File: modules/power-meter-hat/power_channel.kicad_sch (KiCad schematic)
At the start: 8 parts, among them J2 Conn_01x02, U2 INA219AxD

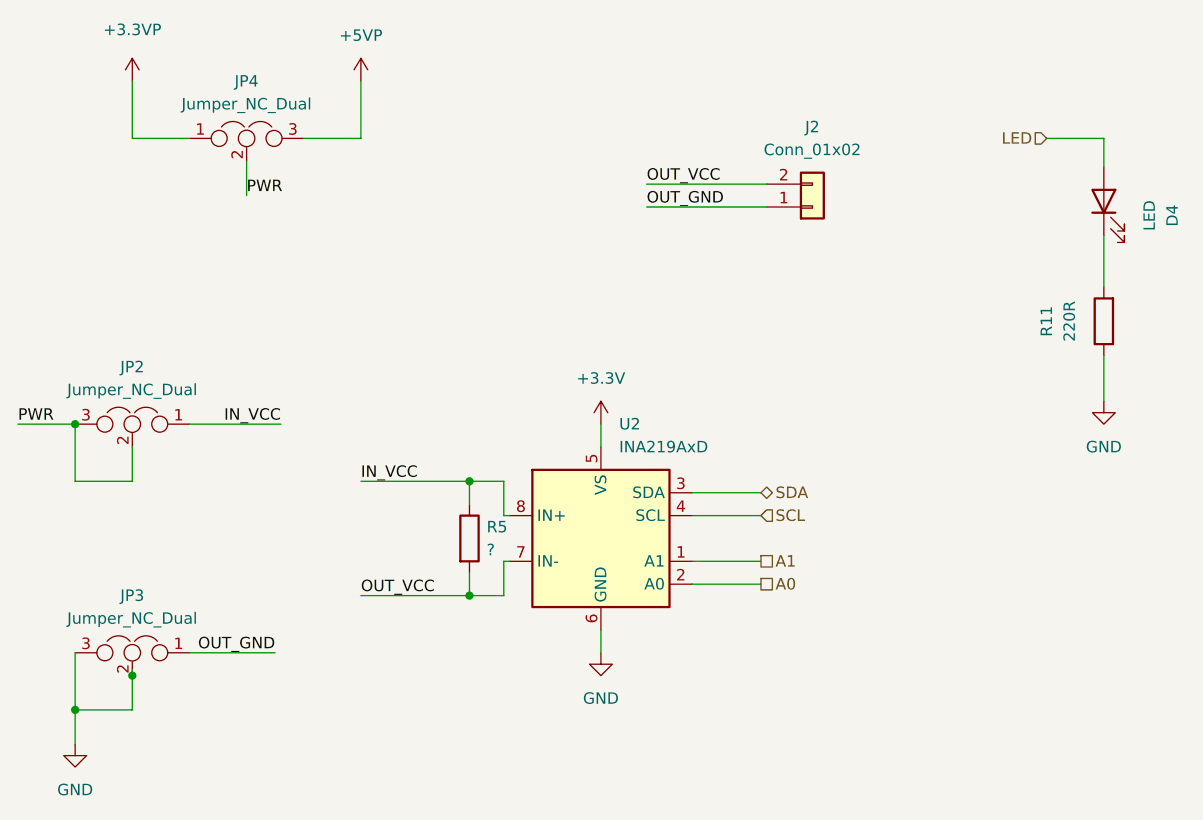
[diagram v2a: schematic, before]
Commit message: Reannotate schematic
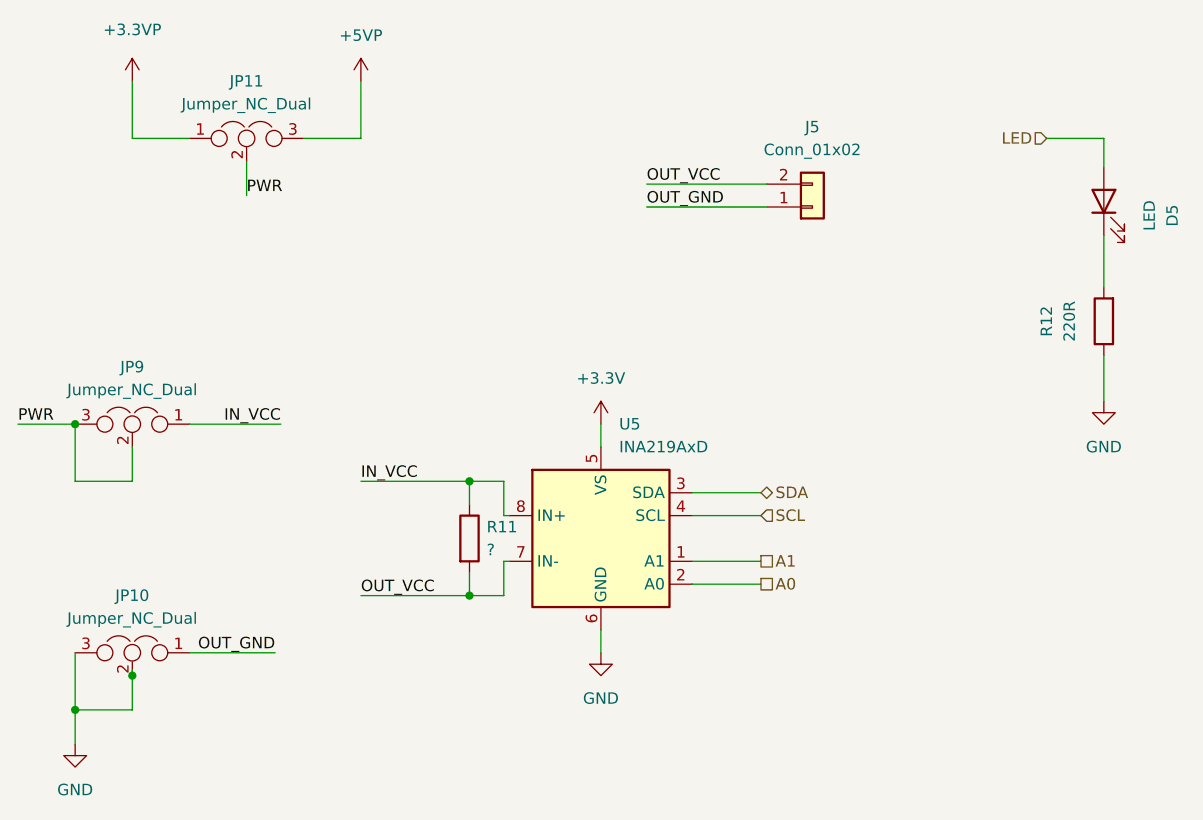
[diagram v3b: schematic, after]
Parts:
- renumbered D4 to D5, J2 to J5, JP3 to JP10, JP4 to JP11, JP2 to JP9, R5 to R11, R11 to R12, U2 to U5
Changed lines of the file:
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@@
   (symbol (lib_id "Device:Jumper_NC_Dual") (at 76.2 63.5 0) (mirror y)
     (in_bom yes) (on_board yes) (fields_autoplaced)
-    (property "Reference" "JP2" (id 0) (at 76.2 57.15 0))
+    (property "Reference" "JP9" (id 0) (at 76.2 57.15 0))
     (property "Value" "Jumper_NC_Dual" (id 1) (at 76.2 59.69 0))
     (property "Footprint" "Connector_PinHeader_2.54mm:PinHeader_1x03_P2.54mm_Vertical" (id 2) (at 76.2 63.5 0)
@@
   (symbol (lib_id "power:+3.3V") (at 128.27 63.5 0)
     (in_bom yes) (on_board yes) (fields_autoplaced)
-    (property "Reference" "#PWR0109" (id 0) (at 128.27 67.31 0)
+    (property "Reference" "#PWR036" (id 0) (at 128.27 67.31 0)
       (effects (font (size 1.27 1.27)) hide)
     )
@@
   (symbol (lib_id "Device:R") (at 113.665 76.2 0)
     (in_bom yes) (on_board yes) (fields_autoplaced)
-    (property "Reference" "R5" (id 0) (at 115.57 74.9299 0)
+    (property "Reference" "R11" (id 0) (at 115.57 74.9299 0)
       (effects (font (size 1.27 1.27)) (justify left))
     )
@@
   (symbol (lib_id "Analog_ADC:INA219AxD") (at 128.27 76.2 0)
     (in_bom yes) (on_board yes) (fields_autoplaced)
-    (property "Reference" "U2" (id 0) (at 130.2894 63.5 0)
+    (property "Reference" "U5" (id 0) (at 130.2894 63.5 0)
       (effects (font (size 1.27 1.27)) (justify left))
     )
@@
   (symbol (lib_id "Device:R") (at 184.15 52.07 180)
     (in_bom yes) (on_board yes) (fields_autoplaced)
-    (property "Reference" "R11" (id 0) (at 177.8 52.07 90))
+    (property "Reference" "R12" (id 0) (at 177.8 52.07 90))
     (property "Value" "220R" (id 1) (at 180.34 52.07 90))
     (property "Footprint" "Resistor_SMD:R_0805_2012Metric_Pad1.20x1.40mm_HandSolder" (id 2) (at 185.928 52.07 90)
@@
   (symbol (lib_id "power:GND") (at 69.85 99.06 0)
     (in_bom yes) (on_board yes) (fields_autoplaced)
-    (property "Reference" "#PWR0113" (id 0) (at 69.85 105.41 0)
+    (property "Reference" "#PWR033" (id 0) (at 69.85 105.41 0)
       (effects (font (size 1.27 1.27)) hide)
     )
@@
   (symbol (lib_id "Connector_Generic:Conn_01x02") (at 151.765 39.37 0) (mirror x)
     (in_bom yes) (on_board yes) (fields_autoplaced)
-    (property "Reference" "J2" (id 0) (at 151.765 30.48 0))
+    (property "Reference" "J5" (id 0) (at 151.765 30.48 0))
     (property "Value" "Conn_01x02" (id 1) (at 151.765 33.02 0))
     (property "Footprint" "TerminalBlock_Phoenix:TerminalBlock_Phoenix_PT-1,5-2-3.5-H_1x02_P3.50mm_Horizontal" (id 2) (at 151.765 39.37 0)
@@
   (symbol (lib_id "power:GND") (at 184.15 60.96 0)
     (in_bom yes) (on_board yes) (fields_autoplaced)
-    (property "Reference" "#PWR0129" (id 0) (at 184.15 67.31 0)
+    (property "Reference" "#PWR038" (id 0) (at 184.15 67.31 0)
       (effects (font (size 1.27 1.27)) hide)
     )
@@
   (symbol (lib_id "Device:Jumper_NC_Dual") (at 88.9 31.75 0)
     (in_bom yes) (on_board yes) (fields_autoplaced)
-    (property "Reference" "JP4" (id 0) (at 88.9 25.4 0))
+    (property "Reference" "JP11" (id 0) (at 88.9 25.4 0))
     (property "Value" "Jumper_NC_Dual" (id 1) (at 88.9 27.94 0))
     (property "Footprint" "Connector_PinHeader_2.54mm:PinHeader_1x03_P2.54mm_Vertical" (id 2) (at 88.9 31.75 0)
@@
   (symbol (lib_id "Device:Jumper_NC_Dual") (at 76.2 88.9 0) (mirror y)
     (in_bom yes) (on_board yes) (fields_autoplaced)
-    (property "Reference" "JP3" (id 0) (at 76.2 82.55 0))
+    (property "Reference" "JP10" (id 0) (at 76.2 82.55 0))
     (property "Value" "Jumper_NC_Dual" (id 1) (at 76.2 85.09 0))
     (property "Footprint" "Connector_PinHeader_2.54mm:PinHeader_1x03_P2.54mm_Vertical" (id 2) (at 76.2 88.9 0)
@@
   (symbol (lib_id "power:+3.3VP") (at 76.2 25.4 0)
     (in_bom yes) (on_board yes) (fields_autoplaced)
-    (property "Reference" "#PWR0111" (id 0) (at 80.01 26.67 0)
+    (property "Reference" "#PWR034" (id 0) (at 80.01 26.67 0)
       (effects (font (size 1.27 1.27)) hide)
     )
@@
   (symbol (lib_id "Device:LED") (at 184.15 38.735 90)
     (in_bom yes) (on_board yes) (fields_autoplaced)
-    (property "Reference" "D4" (id 0) (at 191.77 40.3225 0))
+    (property "Reference" "D5" (id 0) (at 191.77 40.3225 0))
     (property "Value" "LED" (id 1) (at 189.23 40.3225 0))
     (property "Footprint" "LED_SMD:LED_1206_3216Metric_Castellated" (id 2) (at 184.15 38.735 0)
@@
   (symbol (lib_id "power:+5VP") (at 101.6 25.4 0)
     (in_bom yes) (on_board yes) (fields_autoplaced)
-    (property "Reference" "#PWR0112" (id 0) (at 101.6 29.21 0)
+    (property "Reference" "#PWR035" (id 0) (at 101.6 29.21 0)
       (effects (font (size 1.27 1.27)) hide)
     )
@@
   (symbol (lib_id "power:GND") (at 128.27 88.9 0)
     (in_bom yes) (on_board yes) (fields_autoplaced)
-    (property "Reference" "#PWR0110" (id 0) (at 128.27 95.25 0)
+    (property "Reference" "#PWR037" (id 0) (at 128.27 95.25 0)
       (effects (font (size 1.27 1.27)) hide)
     )

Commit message: Replace barrel jack to CLIFF FC68148
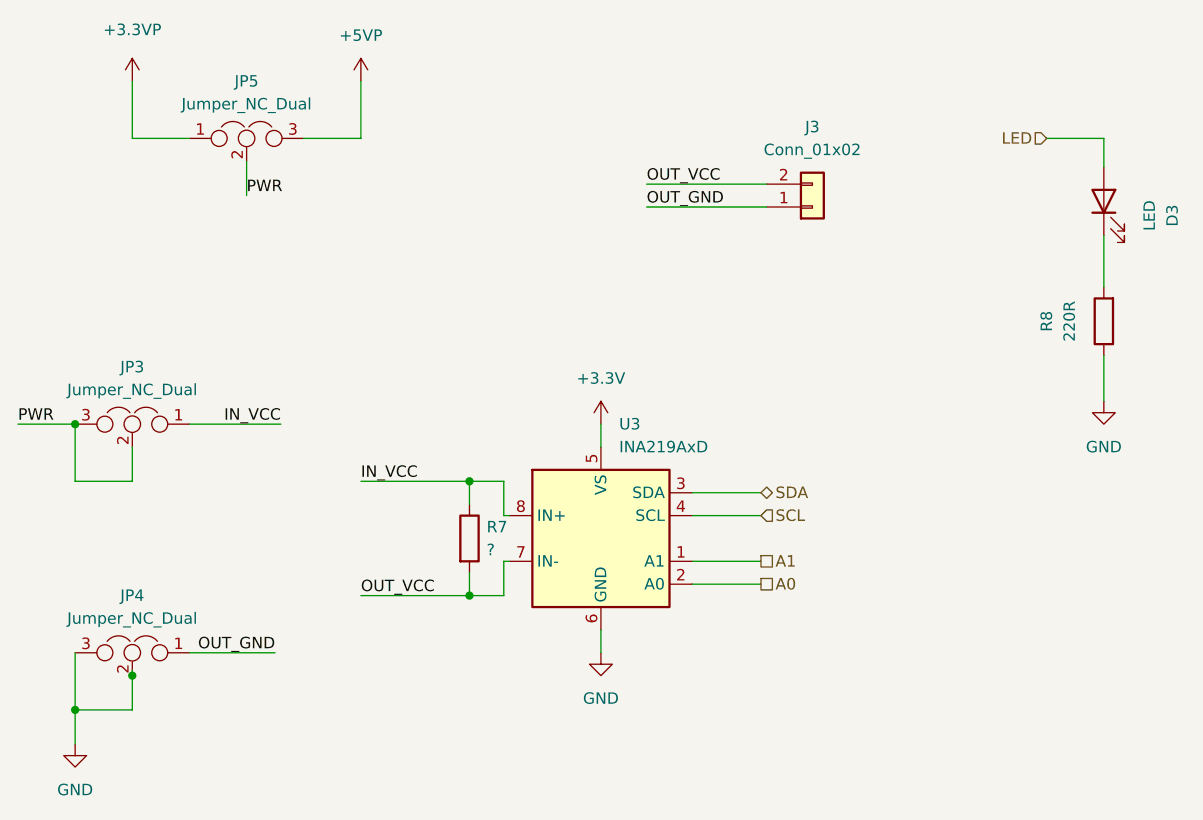
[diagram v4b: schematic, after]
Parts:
- renumbered D5 to D3, J5 to J3, JP9 to JP3, JP10 to JP4, JP11 to JP5, R11 to R7, R12 to R8, U5 to U3
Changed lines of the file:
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@@
   (symbol (lib_id "Device:Jumper_NC_Dual") (at 76.2 63.5 0) (mirror y)
     (in_bom yes) (on_board yes) (fields_autoplaced)
-    (property "Reference" "JP9" (id 0) (at 76.2 57.15 0))
+    (property "Reference" "JP3" (id 0) (at 76.2 57.15 0))
     (property "Value" "Jumper_NC_Dual" (id 1) (at 76.2 59.69 0))
     (property "Footprint" "Connector_PinHeader_2.54mm:PinHeader_1x03_P2.54mm_Vertical" (id 2) (at 76.2 63.5 0)
@@
   (symbol (lib_id "Device:R") (at 113.665 76.2 0)
     (in_bom yes) (on_board yes) (fields_autoplaced)
-    (property "Reference" "R11" (id 0) (at 115.57 74.9299 0)
+    (property "Reference" "R7" (id 0) (at 115.57 74.9299 0)
       (effects (font (size 1.27 1.27)) (justify left))
     )
@@
   (symbol (lib_id "Analog_ADC:INA219AxD") (at 128.27 76.2 0)
     (in_bom yes) (on_board yes) (fields_autoplaced)
-    (property "Reference" "U5" (id 0) (at 130.2894 63.5 0)
+    (property "Reference" "U3" (id 0) (at 130.2894 63.5 0)
       (effects (font (size 1.27 1.27)) (justify left))
     )
@@
   (symbol (lib_id "Device:R") (at 184.15 52.07 180)
     (in_bom yes) (on_board yes) (fields_autoplaced)
-    (property "Reference" "R12" (id 0) (at 177.8 52.07 90))
+    (property "Reference" "R8" (id 0) (at 177.8 52.07 90))
     (property "Value" "220R" (id 1) (at 180.34 52.07 90))
     (property "Footprint" "Resistor_SMD:R_0805_2012Metric_Pad1.20x1.40mm_HandSolder" (id 2) (at 185.928 52.07 90)
@@
   (symbol (lib_id "Connector_Generic:Conn_01x02") (at 151.765 39.37 0) (mirror x)
     (in_bom yes) (on_board yes) (fields_autoplaced)
-    (property "Reference" "J5" (id 0) (at 151.765 30.48 0))
+    (property "Reference" "J3" (id 0) (at 151.765 30.48 0))
     (property "Value" "Conn_01x02" (id 1) (at 151.765 33.02 0))
     (property "Footprint" "TerminalBlock_Phoenix:TerminalBlock_Phoenix_PT-1,5-2-3.5-H_1x02_P3.50mm_Horizontal" (id 2) (at 151.765 39.37 0)
@@
   (symbol (lib_id "Device:Jumper_NC_Dual") (at 88.9 31.75 0)
     (in_bom yes) (on_board yes) (fields_autoplaced)
-    (property "Reference" "JP11" (id 0) (at 88.9 25.4 0))
+    (property "Reference" "JP5" (id 0) (at 88.9 25.4 0))
     (property "Value" "Jumper_NC_Dual" (id 1) (at 88.9 27.94 0))
     (property "Footprint" "Connector_PinHeader_2.54mm:PinHeader_1x03_P2.54mm_Vertical" (id 2) (at 88.9 31.75 0)
@@
   (symbol (lib_id "Device:Jumper_NC_Dual") (at 76.2 88.9 0) (mirror y)
     (in_bom yes) (on_board yes) (fields_autoplaced)
-    (property "Reference" "JP10" (id 0) (at 76.2 82.55 0))
+    (property "Reference" "JP4" (id 0) (at 76.2 82.55 0))
     (property "Value" "Jumper_NC_Dual" (id 1) (at 76.2 85.09 0))
     (property "Footprint" "Connector_PinHeader_2.54mm:PinHeader_1x03_P2.54mm_Vertical" (id 2) (at 76.2 88.9 0)
@@
   (symbol (lib_id "Device:LED") (at 184.15 38.735 90)
     (in_bom yes) (on_board yes) (fields_autoplaced)
-    (property "Reference" "D5" (id 0) (at 191.77 40.3225 0))
+    (property "Reference" "D3" (id 0) (at 191.77 40.3225 0))
     (property "Value" "LED" (id 1) (at 189.23 40.3225 0))
     (property "Footprint" "LED_SMD:LED_1206_3216Metric_Castellated" (id 2) (at 184.15 38.735 0)

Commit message: Move jumpers to bottom side & other improvements
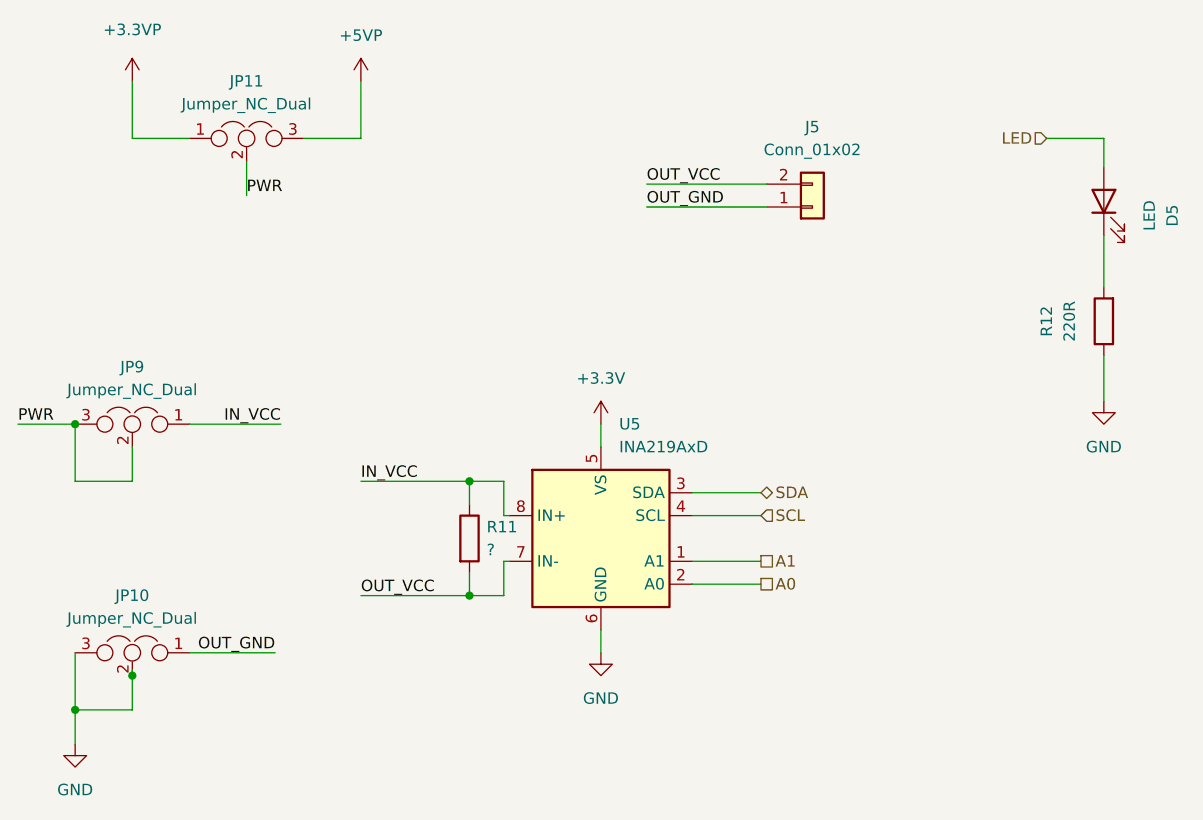
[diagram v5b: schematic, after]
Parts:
- renumbered D3 to D5, J3 to J5, JP4 to JP10, JP5 to JP11, JP3 to JP9, R7 to R11, R8 to R12, U3 to U5
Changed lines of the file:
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@@
   (symbol (lib_id "Device:Jumper_NC_Dual") (at 76.2 63.5 0) (mirror y)
     (in_bom yes) (on_board yes) (fields_autoplaced)
-    (property "Reference" "JP3" (id 0) (at 76.2 57.15 0))
+    (property "Reference" "JP9" (id 0) (at 76.2 57.15 0))
     (property "Value" "Jumper_NC_Dual" (id 1) (at 76.2 59.69 0))
     (property "Footprint" "Connector_PinHeader_2.54mm:PinHeader_1x03_P2.54mm_Vertical" (id 2) (at 76.2 63.5 0)
@@
   (symbol (lib_id "Device:R") (at 113.665 76.2 0)
     (in_bom yes) (on_board yes) (fields_autoplaced)
-    (property "Reference" "R7" (id 0) (at 115.57 74.9299 0)
+    (property "Reference" "R11" (id 0) (at 115.57 74.9299 0)
       (effects (font (size 1.27 1.27)) (justify left))
     )
@@
   (symbol (lib_id "Analog_ADC:INA219AxD") (at 128.27 76.2 0)
     (in_bom yes) (on_board yes) (fields_autoplaced)
-    (property "Reference" "U3" (id 0) (at 130.2894 63.5 0)
+    (property "Reference" "U5" (id 0) (at 130.2894 63.5 0)
       (effects (font (size 1.27 1.27)) (justify left))
     )
@@
   (symbol (lib_id "Device:R") (at 184.15 52.07 180)
     (in_bom yes) (on_board yes) (fields_autoplaced)
-    (property "Reference" "R8" (id 0) (at 177.8 52.07 90))
+    (property "Reference" "R12" (id 0) (at 177.8 52.07 90))
     (property "Value" "220R" (id 1) (at 180.34 52.07 90))
     (property "Footprint" "Resistor_SMD:R_0805_2012Metric_Pad1.20x1.40mm_HandSolder" (id 2) (at 185.928 52.07 90)
@@
   (symbol (lib_id "Connector_Generic:Conn_01x02") (at 151.765 39.37 0) (mirror x)
     (in_bom yes) (on_board yes) (fields_autoplaced)
-    (property "Reference" "J3" (id 0) (at 151.765 30.48 0))
+    (property "Reference" "J5" (id 0) (at 151.765 30.48 0))
     (property "Value" "Conn_01x02" (id 1) (at 151.765 33.02 0))
     (property "Footprint" "TerminalBlock_Phoenix:TerminalBlock_Phoenix_PT-1,5-2-3.5-H_1x02_P3.50mm_Horizontal" (id 2) (at 151.765 39.37 0)
@@
   (symbol (lib_id "Device:Jumper_NC_Dual") (at 88.9 31.75 0)
     (in_bom yes) (on_board yes) (fields_autoplaced)
-    (property "Reference" "JP5" (id 0) (at 88.9 25.4 0))
+    (property "Reference" "JP11" (id 0) (at 88.9 25.4 0))
     (property "Value" "Jumper_NC_Dual" (id 1) (at 88.9 27.94 0))
     (property "Footprint" "Connector_PinHeader_2.54mm:PinHeader_1x03_P2.54mm_Vertical" (id 2) (at 88.9 31.75 0)
@@
   (symbol (lib_id "Device:Jumper_NC_Dual") (at 76.2 88.9 0) (mirror y)
     (in_bom yes) (on_board yes) (fields_autoplaced)
-    (property "Reference" "JP4" (id 0) (at 76.2 82.55 0))
+    (property "Reference" "JP10" (id 0) (at 76.2 82.55 0))
     (property "Value" "Jumper_NC_Dual" (id 1) (at 76.2 85.09 0))
     (property "Footprint" "Connector_PinHeader_2.54mm:PinHeader_1x03_P2.54mm_Vertical" (id 2) (at 76.2 88.9 0)
@@
   (symbol (lib_id "Device:LED") (at 184.15 38.735 90)
     (in_bom yes) (on_board yes) (fields_autoplaced)
-    (property "Reference" "D3" (id 0) (at 191.77 40.3225 0))
+    (property "Reference" "D5" (id 0) (at 191.77 40.3225 0))
     (property "Value" "LED" (id 1) (at 189.23 40.3225 0))
     (property "Footprint" "LED_SMD:LED_1206_3216Metric_Castellated" (id 2) (at 184.15 38.735 0)
